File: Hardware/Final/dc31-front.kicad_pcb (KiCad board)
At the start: 2 copper layers, 111.4 x 128.5 mm, 0 parts

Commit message: Almost final, still need some artwork
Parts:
- added D101: WS2812B, lib_fp:LED_SK6812_4020_, B.Cu at (180.8, 149.0)
- added D102: WS2812B, lib_fp:LED_SK6812_4020_, B.Cu at (161.8, 149.0)
- added D103: WS2812B, lib_fp:LED_SK6812_4020_, B.Cu at (142.8, 149.0)
- added D104: WS2812B, lib_fp:LED_SK6812_4020_, B.Cu at (123.8, 149.0)
- added D105: WS2812B, lib_fp:LED_SK6812_4020_, B.Cu at (124.2, 108.2)
- added D106: WS2812B, lib_fp:LED_SK6812_4020_, B.Cu at (143.2, 108.2)
- added D107: WS2812B, lib_fp:LED_SK6812_4020_, B.Cu at (162.2, 108.2)
- added D108: WS2812B, lib_fp:LED_SK6812_4020_, B.Cu at (181.2, 108.2)
- added D109: WS2812B, lib_fp:LED_SK6812_4020_, B.Cu at (124.2, 82.2)
- added D110: WS2812B, lib_fp:LED_SK6812_4020_, B.Cu at (143.2, 82.2)
- added J101: FRONT, Connector_PinSocket_2.54mm:PinSocket_1x04_P2.54mm_Vertical_SMD_Pin1Left, B.Cu at (197.0, 143.5)
- added R101: 10R, Resistor_SMD:R_0603_1608Metric, B.Cu at (189.3, 150.9)
- added REF**: Speaker, lib_fp:Speaker, B.Cu at (105.6, 70.6)
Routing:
- net +3V3: track 0.00 -> 302.9 mm
- net Net-(D108-DOUT): track 0.00 -> 102.6 mm
- net Net-(D104-DOUT): track 0.00 -> 68.6 mm
- net Net-(D102-DOUT): track 0.00 -> 19.8 mm
- net Net-(D103-DOUT): track 0.00 -> 19.7 mm
- net Net-(D101-DOUT): track 0.00 -> 19.7 mm
- net Net-(D106-DOUT): track 0.00 -> 19.6 mm
- net Net-(D107-DOUT): track 0.00 -> 19.6 mm
- net Net-(D105-DOUT): track 0.00 -> 19.5 mm
- net Net-(D109-DOUT): track 0.00 -> 18.4 mm
- net Net-(J101-Pin_4): track 0.00 -> 6.70 mm
- net Net-(D101-DIN): track 0.00 -> 6.45 mm
- added copper zone on F.Cu, net (none)
- added copper zone on B.Cu, net GND
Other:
- outline, holes or cut-outs redrawn
- board text added: "@hamster@fosstodon.org"

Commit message: Adding SAO port to front panel Adding hamster art to boards A few more small tweaks before final export
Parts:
- added C101: 0.1uF, Capacitor_SMD:C_0603_1608Metric, B.Cu at (192.3, 153.2)
- added C102: 0.1uF, Capacitor_SMD:C_0603_1608Metric, B.Cu at (152.9, 106.7)
- added C103: 0.1uF, Capacitor_SMD:C_0603_1608Metric, B.Cu at (133.2, 78.2)
- added G***: LOGO, lib_fp:hamster, B.Cu at (105.6, 128.0)
- added X101: Badgelife_sao_connector_v169bis, lib_fp:Badgelife-Shitty-v1.69bis, F.Cu at (197.7, 103.5)
- J101: footprint Connector_PinSocket_2.54mm:PinSocket_1x04_P2.54mm_Vertical_SMD_Pin1Left -> Connector_PinSocket_2.54mm:PinSocket_1x05_P2.54mm_Vertical_SMD_Pin1Left
- moved J101 1.27 mm to (197.0, 144.8)
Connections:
- J101 pad 1: GND -> +3V3
- J101 pad 2: +3V3 -> GND
- J101 pad 3: unconnected-(J101-Pin_3-Pad3) -> SDA
- J101 pad 4: Net-(J101-Pin_4) -> SCL
- R101 pad 2: Net-(J101-Pin_4) -> Net-(J101-Pin_5)
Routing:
- net +3V3: track 302.9 -> 371.0 mm
- net SCL: track 0.00 -> 47.4 mm
- net SDA: track 0.00 -> 43.8 mm
- net Net-(J101-Pin_5): track 0.00 -> 8.87 mm
- net Net-(J101-Pin_4): track 6.70 -> 0.00 mm

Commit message: Final files as submitted to fab
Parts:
- moved G*** 0.50 mm to (105.2, 127.8)
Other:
- board text added: "ALL FAB MARKS ON BOTTOM LAYER"
- board text added: "DCZia Electric Sampler"
- board text added: "Design by DCZia Team 2023"
- board text added: "github.com/dczia/Defcon31-Badge"
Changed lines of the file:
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@@
     (pad_to_mask_clearance 0)
     (pcbplotparams
-      (layerselection 0x00010fc_ffffffff)
+      (layerselection 0x00310fc_ffffffff)
       (plot_on_all_layers_selection 0x0000000_00000000)
       (disableapertmacros false)
@@
       (plotinvisibletext false)
       (sketchpadsonfab false)
-      (subtractmaskfromsilk true)
-      (outputformat 1)
+      (subtractmaskfromsilk false)
+      (outputformat 4)
       (mirror false)
       (drillshape 0)
@@
   )
   (footprint "lib_fp:hamster" (layer "B.Cu")
-    (at 105.61 127.995 180)
+    (at 105.167809 127.766977 180)
     (attr board_only exclude_from_pos_files exclude_from_bom)
     (fp_text reference "G***" (at 0 0) (layer "B.SilkS") hide
@@
   (gr_circle (center 123.71 70.56) (end 131.51 70.56)
     (stroke (width 0.2) (type default)) (fill none) (layer "Edge.Cuts"))
-  (gr_text "@hamster@fosstodon.org" (at 100.15 113.68 90) (layer "B.Cu")
-    (effects (font (size 1.5 1.5) (thickness 0.3) bold) (justify left bottom mirror))
+  (gr_text "@hamster@fosstodon.org" (at 99.865 118.185 90) (layer "B.Cu")
+    (effects (font (size 1 1) (thickness 0.15)) (justify left bottom mirror))
+  )
+  (gr_text "Design by DCZia Team 2023" (at 204.395 92.845) (layer "B.SilkS")
+    (effects (font (size 2 2) (thickness 0.2)) (justify left bottom mirror))
+  )
+  (gr_text "DCZia Electric Sampler" (at 204.415 90.09) (layer "B.SilkS")
+    (effects (font (size 2 2) (thickness 0.2)) (justify left bottom mirror))
+  )
+  (gr_text "github.com/dczia/Defcon31-Badge" (at 204.35 95.815) (layer "B.SilkS")
+    (effects (font (size 1.8 1.8) (thickness 0.2)) (justify left bottom mirror))
+  )
+  (gr_text "ALL FAB MARKS\nON BOTTOM LAYER" (at 179.975 88.035) (layer "B.Fab")
+    (effects (font (size 3 3) (thickness 0.35)) (justify bottom mirror))
   )
   (segment (start 111.33 105.897401) (end 111.33 104.822598) (width 0.381) (layer "B.Cu") (net 2))

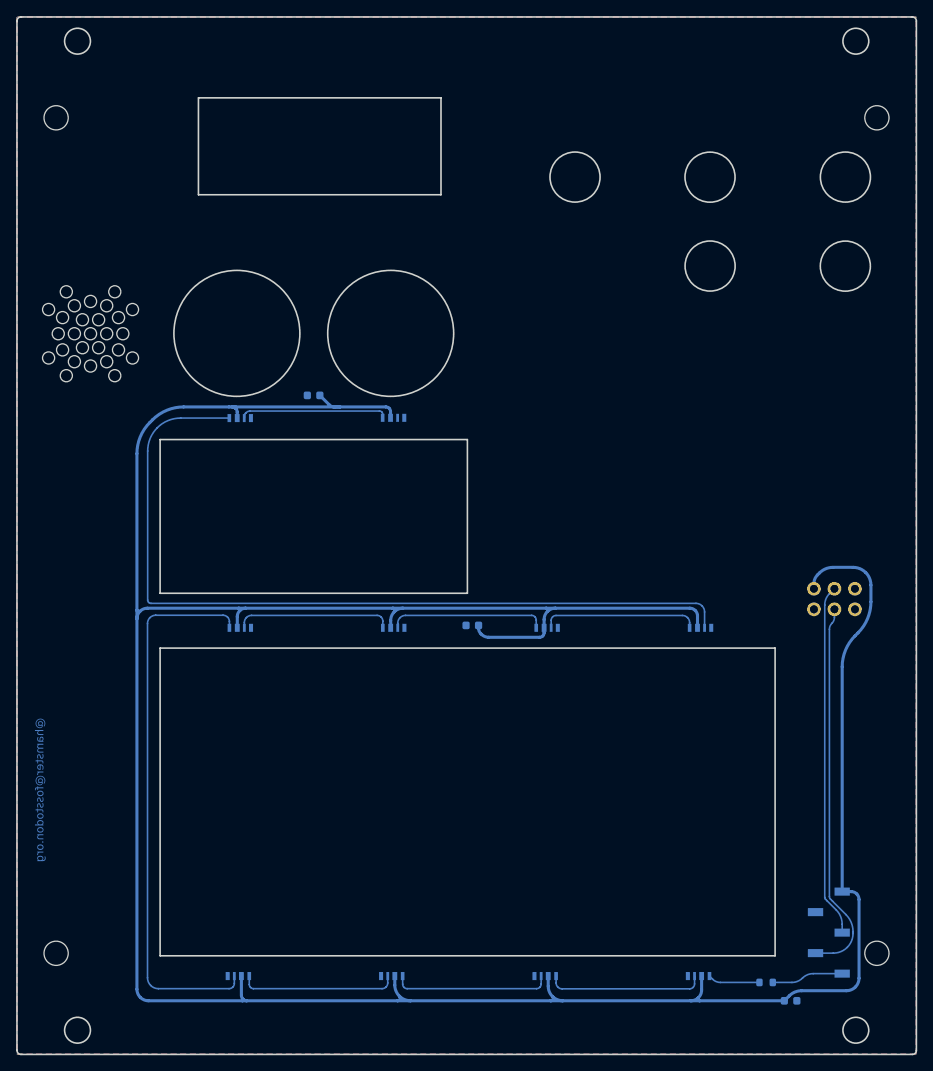
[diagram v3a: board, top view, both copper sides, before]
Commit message: Updated some 3D models Updated BOM sheet Added bodge instructions Added some documentation
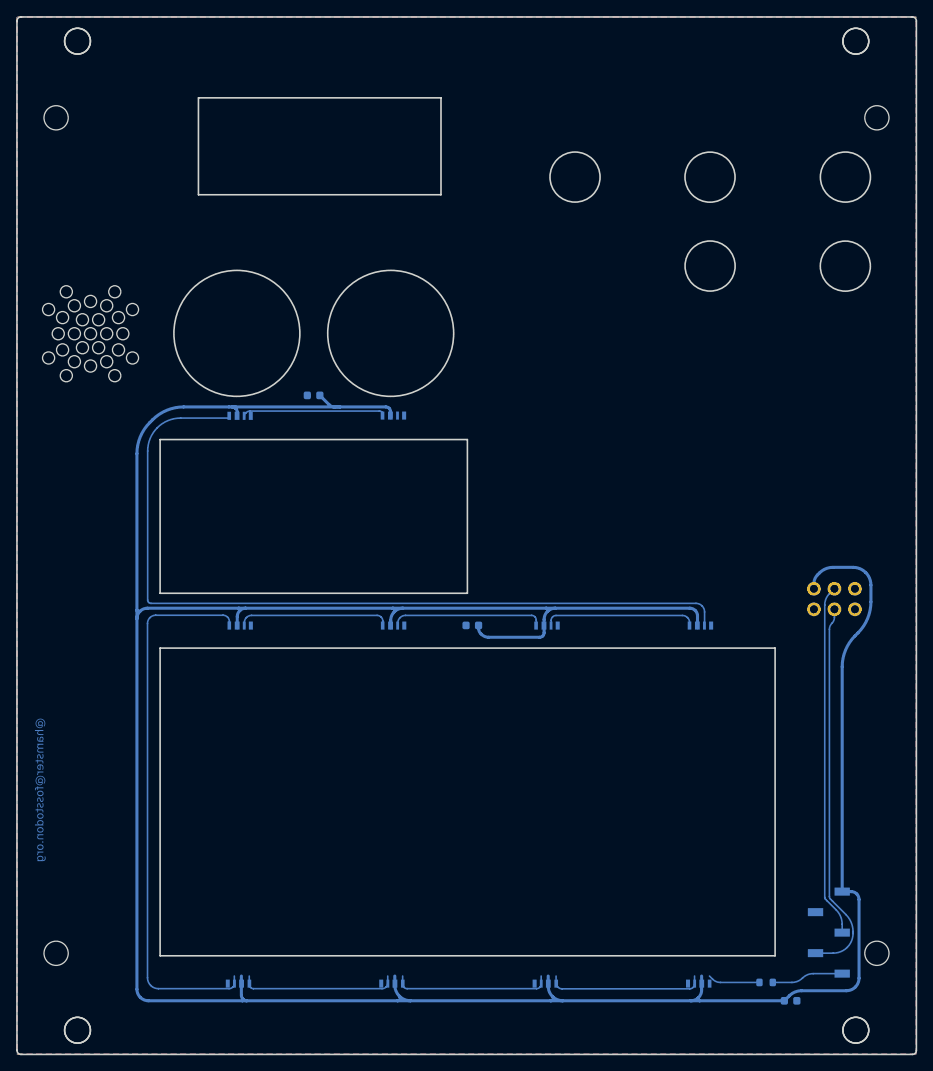
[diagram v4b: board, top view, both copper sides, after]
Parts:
- added HOLE1: MountingHole_1.6, lib_fp:MountingHole_1.6, F.Cu at (104.0, 34.4)
- added HOLE2: MountingHole_1.6, lib_fp:MountingHole_1.6, F.Cu at (200.4, 34.4)
- added HOLE3: MountingHole_1.6, lib_fp:MountingHole_1.6, F.Cu at (104.0, 156.9)
- added HOLE4: MountingHole_1.6, lib_fp:MountingHole_1.6, F.Cu at (200.4, 156.9)
- moved D101 2.11 mm to (180.9, 151.1)
- moved D102 2.11 mm to (161.9, 151.1)
- moved D103 2.11 mm to (142.9, 151.1)
- moved D104 2.11 mm to (123.9, 151.1)
- moved D109 1.45 mm to (124.1, 80.8)
- moved D110 1.45 mm to (143.1, 80.8)
- moved D105 1.45 mm to (124.1, 106.8)
- moved D106 1.45 mm to (143.1, 106.8)
- moved D107 1.45 mm to (162.1, 106.8)
- moved D108 1.45 mm to (181.1, 106.8)
